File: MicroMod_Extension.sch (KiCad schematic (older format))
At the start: 80 parts, among them J1 2199230-4, J10 Conn_01x02, J11 Screw_Terminal_01x04, J2 XKB_U262-16XN-4BVC11, J3 RSP-122811-01, J4 Screw_Terminal_01x04, J5 Conn_01x08, J6 Conn_01x08, J7 Conn_01x04, J8 Conn_01x04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

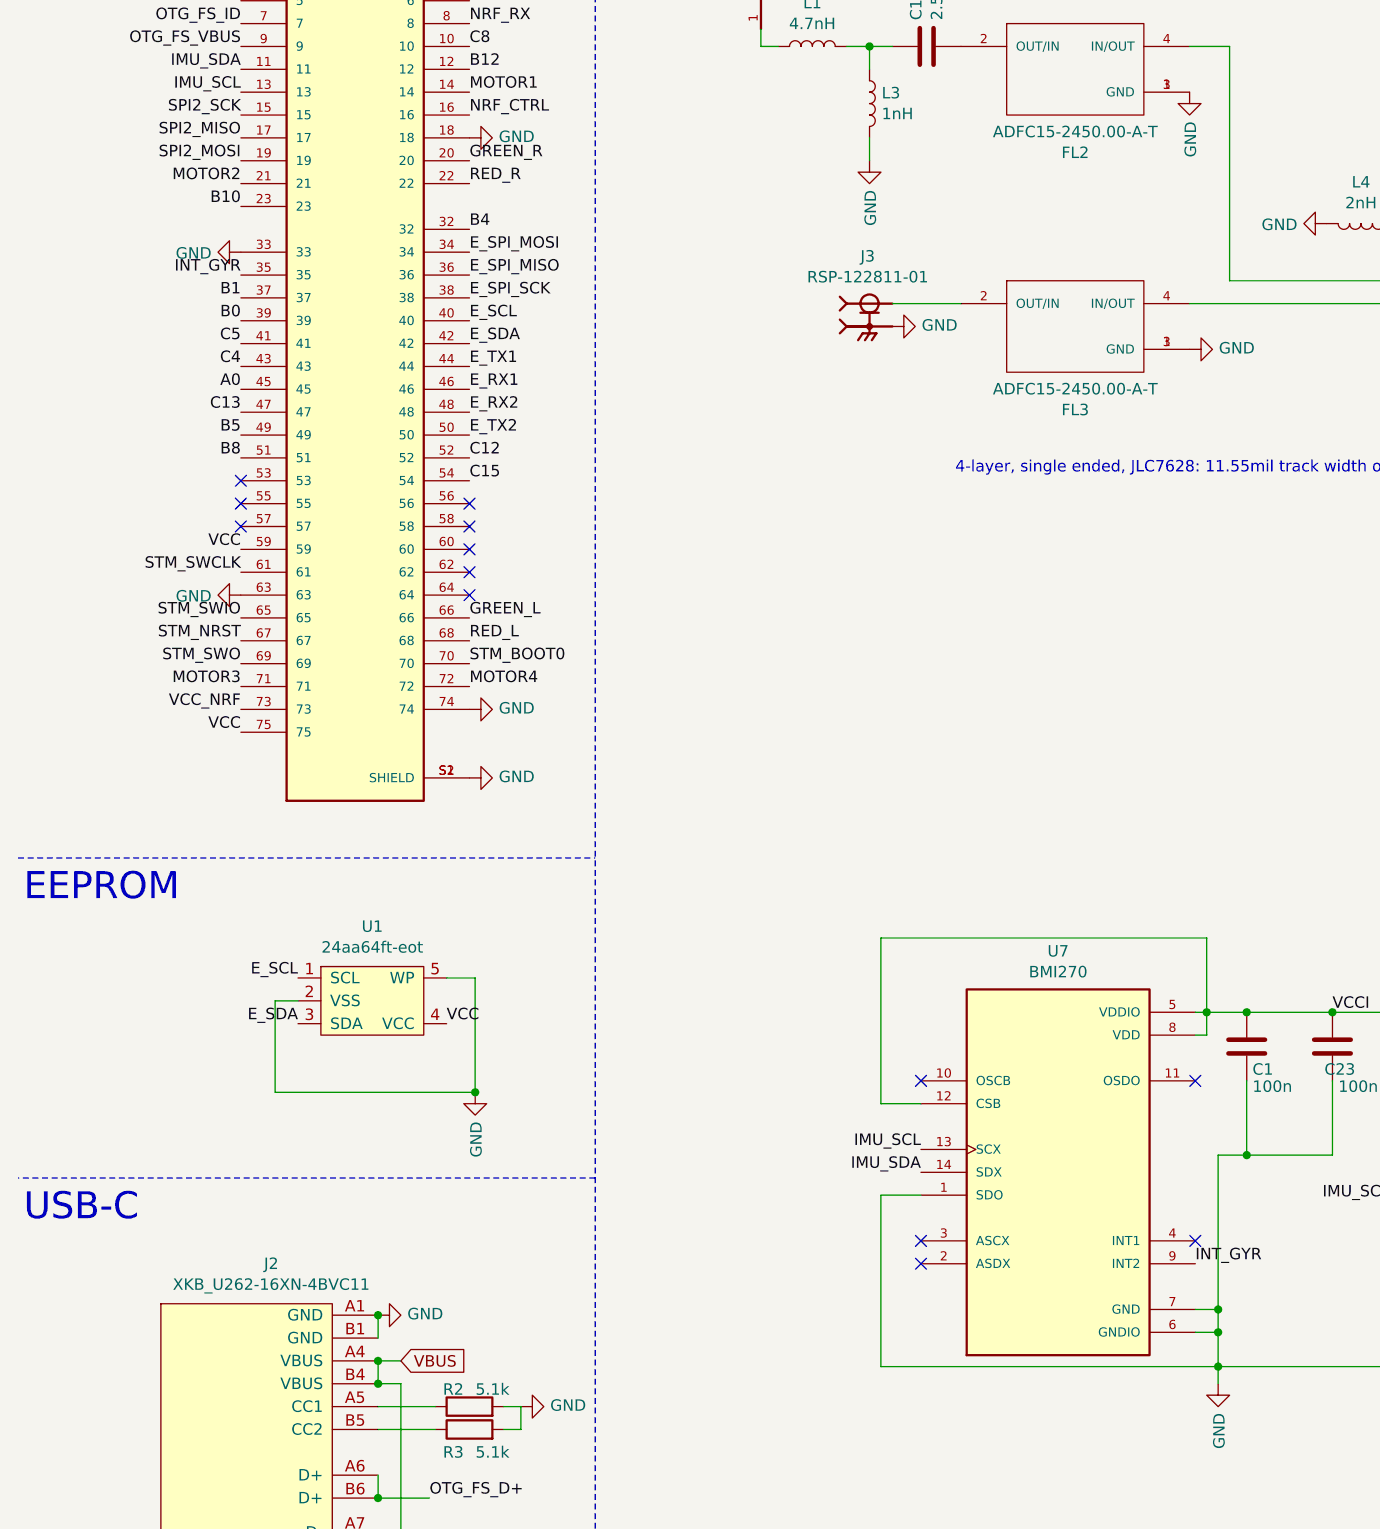
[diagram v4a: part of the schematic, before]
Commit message: change motor2 and motor4
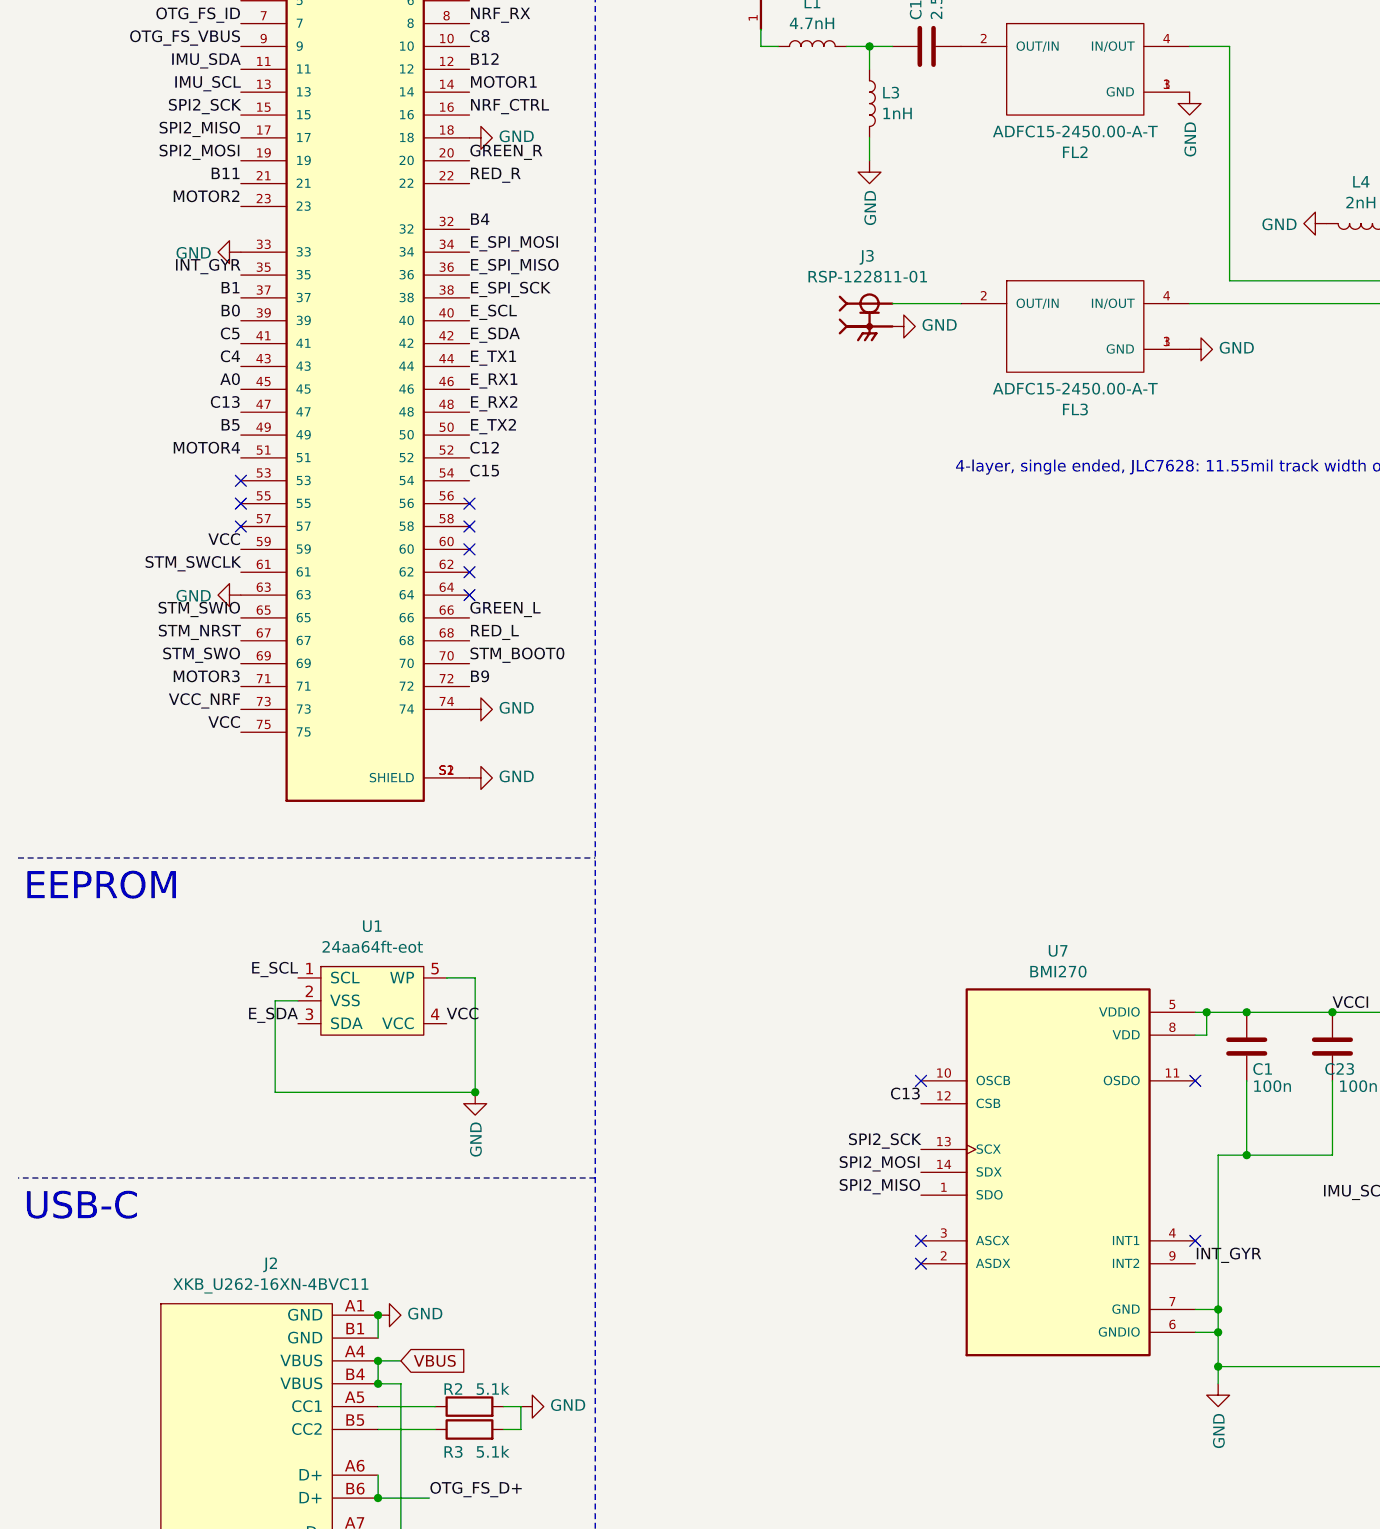
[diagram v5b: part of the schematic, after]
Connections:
- net B10 is gone; now on net MOTOR2: J1.23
- net B8 is gone; now on net MOTOR4: J1.51
- net C13: now also U7.12 (CSB)
- net GND: no longer U7.1 (SDO)
- net IMU_SCL: no longer U7.13 (SCX)
- net IMU_SDA: no longer U7.14 (SDX)
- net MOTOR2: no longer J1.21
- net MOTOR4: no longer J1.72
- net SPI2_MISO: now also U7.1 (SDO)
- net SPI2_MOSI: now also U7.14 (SDX)
- net SPI2_SCK: now also U7.13 (SCX)
- net VCCI: no longer U7.12 (CSB)
- new net B11: J1.21
- new net B9: J1.72
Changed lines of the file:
@@
 SPI2_MOSI
 Text Label 1450 2050 2    50   ~ 0
+B11
+Text Label 1450 2150 2    50   ~ 0
 MOTOR2
-Text Label 1450 2150 2    50   ~ 0
-B10
 Text Label 1450 2450 2    50   ~ 0
 INT_GYR
@@
 B5
 Text Label 1450 3250 2    50   ~ 0
-B8
+MOTOR4
 Text Label 1450 3650 2    50   ~ 0
 VCC
@@
 VCC
 Text Label 2450 4250 0    50   ~ 0
-MOTOR4
+B9
 Text Label 2450 4150 0    50   ~ 0
 STM_BOOT0
@@
 NoConn ~ 12050 2825
 NoConn ~ 12050 1925
-$Comp
-L MicroMod_Extension:BMI270 U7
-U 1 1 6196DC76
-P 5025 6375
-F 0 "U7" H 5025 7342 50  0000 C CNN
-F 1 "BMI270" H 5025 7251 50  0000 C CNN
-F 2 "XDCR_BMI270" H 5025 6375 50  0001 L BNN
-F 3 "" H 5025 6375 50  0001 L BNN
-F 4 "Bosch Sensortec" H 5025 6375 50  0001 L BNN "MANUFACTURER"
-F 5 "1.0" H 5025 6375 50  0001 L BNN "PATREV"
-F 6 "0.87mm" H 5025 6375 50  0001 L BNN "MAXIMUM_PACKAGE_HEIGHT"
-F 7 "Manufacturer Recommendations" H 5025 6375 50  0001 L BNN "STANDARD"
-	1    5025 6375
-	1    0    0    -1
-$EndComp
 NoConn ~ 5625 5975
 NoConn ~ 4425 5975
@@
 Wire Wire Line
 	5675 5775 5675 5675
-Wire Wire Line
-	4425 6075 4250 6075
-Wire Wire Line
-	4250 6075 4250 5350
-Wire Wire Line
-	4250 5350 5675 5350
-Wire Wire Line
-	5675 5350 5675 5675
 Text Label 4425 6375 2    50   ~ 0
-IMU_SDA
+SPI2_MOSI
 Text Label 4425 6275 2    50   ~ 0
-IMU_SCL
-Wire Wire Line
-	4425 6475 4250 6475
-Wire Wire Line
-	4250 6475 4250 7225
-Wire Wire Line
-	4250 7225 5725 7225
+SPI2_SCK
 Connection ~ 5725 7225
 Wire Wire Line
@@
 	1    0    0    -1
 $EndComp
+Text Label 4425 6475 2    50   ~ 0
+SPI2_MISO
+$Comp
+L MicroMod_Extension:BMI270 U7
+U 1 1 6196DC76
+P 5025 6375
+F 0 "U7" H 5025 7342 50  0000 C CNN
+F 1 "BMI270" H 5025 7251 50  0000 C CNN
+F 2 "XDCR_BMI270" H 5025 6375 50  0001 L BNN
+F 3 "" H 5025 6375 50  0001 L BNN
+F 4 "Bosch Sensortec" H 5025 6375 50  0001 L BNN "MANUFACTURER"
+F 5 "1.0" H 5025 6375 50  0001 L BNN "PATREV"
+F 6 "0.87mm" H 5025 6375 50  0001 L BNN "MAXIMUM_PACKAGE_HEIGHT"
+F 7 "Manufacturer Recommendations" H 5025 6375 50  0001 L BNN "STANDARD"
+	1    5025 6375
+	1    0    0    -1
+$EndComp
+Text Label 4425 6075 2    50   ~ 0
+C13
 $EndSCHEMATC

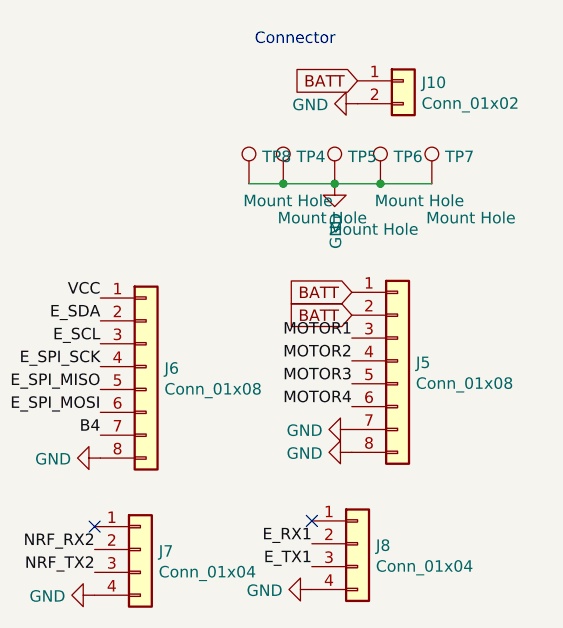
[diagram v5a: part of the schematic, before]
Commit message: change to iflight esc connection
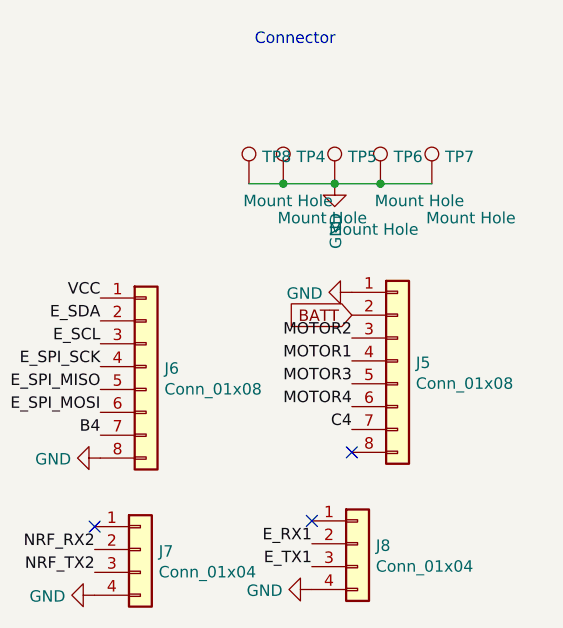
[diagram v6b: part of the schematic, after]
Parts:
- removed J10: Conn_01x02, MicroMod_Extension:BATTARY, symbol Connector_Generic:Conn_01x02
- J5: footprint Connector_JST:JST_SUR_BM08B-SURS-TF_1x08-1MP_P0.80mm_Vertical -> Connector_JST:JST_SH_SM08B-SRSS-TB_1x08-1MP_P1.00mm_Horizontal
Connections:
- net BATT: no longer J5.1 (Pin_1)
- net C4: now also J5.7 (Pin_7)
- net GND: now also J5.1 (Pin_1); no longer J5.7 (Pin_7), J5.8 (Pin_8)
- net MOTOR1: now also J5.4 (Pin_4); no longer J5.3 (Pin_3)
- net MOTOR2: now also J5.3 (Pin_3); no longer J5.4 (Pin_4)
- no-connect marks 40 -> 41
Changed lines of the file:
@@
 F 0 "J5" H 15505 1967 50  0000 L CNN
 F 1 "Conn_01x08" H 15505 1876 50  0000 L CNN
-F 2 "Connector_JST:JST_SUR_BM08B-SURS-TF_1x08-1MP_P0.80mm_Vertical" H 15425 1975 50  0001 C CNN
+F 2 "Connector_JST:JST_SH_SM08B-SRSS-TB_1x08-1MP_P1.00mm_Horizontal" H 15425 1975 50  0001 C CNN
 F 3 "~" H 15425 1975 50  0001 C CNN
 	1    15425 1975
@@
 VCC
 $Comp
-L power:GND #PWR0135
-U 1 1 619F4806
-P 15225 2375
-F 0 "#PWR0135" H 15225 2125 50  0001 C CNN
-F 1 "GND" V 15230 2247 50  0000 R CNN
-F 2 "" H 15225 2375 50  0001 C CNN
-F 3 "" H 15225 2375 50  0001 C CNN
-	1    15225 2375
-	0    1    1    0
-$EndComp
-$Comp
 L power:GND #PWR0136
 U 1 1 61A085B5
@@
 $EndComp
 Text Label 15225 1875 2    50   ~ 0
+MOTOR2
+Text Label 15225 1975 2    50   ~ 0
 MOTOR1
-Text Label 15225 1975 2    50   ~ 0
-MOTOR2
 Text Label 15225 2075 2    50   ~ 0
 MOTOR3
@@
 Text Label 14125 2300 2    50   ~ 0
 B4
-Text GLabel 15225 1675 0    50   Input ~ 0
-BATT
 Text GLabel 15225 1775 0    50   Input ~ 0
 BATT
@@
 L power:GND #PWR0137
 U 1 1 61BD4FBC
-P 15225 2275
-F 0 "#PWR0137" H 15225 2025 50  0001 C CNN
-F 1 "GND" V 15230 2147 50  0000 R CNN
-F 2 "" H 15225 2275 50  0001 C CNN
-F 3 "" H 15225 2275 50  0001 C CNN
-	1    15225 2275
+P 15225 1675
+F 0 "#PWR0137" H 15225 1425 50  0001 C CNN
+F 1 "GND" V 15230 1547 50  0000 R CNN
+F 2 "" H 15225 1675 50  0001 C CNN
+F 3 "" H 15225 1675 50  0001 C CNN
+	1    15225 1675
 	0    1    1    0
 $EndComp
@@
 	1    0    0    -1
 $EndComp
-$Comp
-L Connector_Generic:Conn_01x02 J10
-U 1 1 61893954
-P 15450 750
-F 0 "J10" H 15530 742 50  0000 L CNN
-F 1 "Conn_01x02" H 15530 651 50  0000 L CNN
-F 2 "MicroMod_Extension:BATTARY" H 15450 750 50  0001 C CNN
-F 3 "~" H 15450 750 50  0001 C CNN
-	1    15450 750
-	1    0    0    -1
-$EndComp
-$Comp
-L power:GND #PWR0141
-U 1 1 61894E7F
-P 15250 850
-F 0 "#PWR0141" H 15250 600 50  0001 C CNN
-F 1 "GND" V 15255 722 50  0000 R CNN
-F 2 "" H 15250 850 50  0001 C CNN
-F 3 "" H 15250 850 50  0001 C CNN
-	1    15250 850
-	0    1    1    0
-$EndComp
-Text GLabel 15250 750  0    50   Input ~ 0
-BATT
 $Comp
 L power:GND #PWR0142
@@
 Text Label 4425 6075 2    50   ~ 0
 C13
+Text Label 15225 2275 2    50   ~ 0
+C4
+NoConn ~ 15225 2375
 $EndSCHEMATC
